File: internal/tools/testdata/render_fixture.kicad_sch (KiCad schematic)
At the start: 3 parts

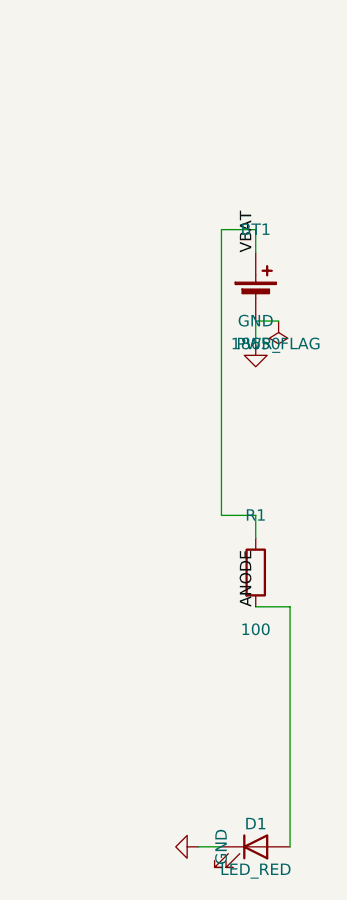
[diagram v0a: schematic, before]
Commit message: Prune projects/ down to the live compiled corpus
The F4 cutover retired the algorithmic pipeline but left its output
behind: 24 project directories from May and July whose only producer no
longer exists. What survives is projects/compiled_* — the seven
reference circuits built from docs/compiler/*.design.json — plus the
gitignored *_e2e output of verify_e2e.

Two tests were reading fixtures out of that rubble and would have gone
silently green via t.Skip once it was gone. TestRenderSchematicPNG now
uses internal/tools/testdata/render_fixture.kicad_sch instead of
projects/inv_amp_v2; TestBodyBBoxNeverSwallowsAPin keeps globbing
compiled_*, which is why that directory stays versioned.

Both verified to run rather than skip.

Co-Authored-By: Claude Opus 5 (1M context) <noreply@anthropic.com>
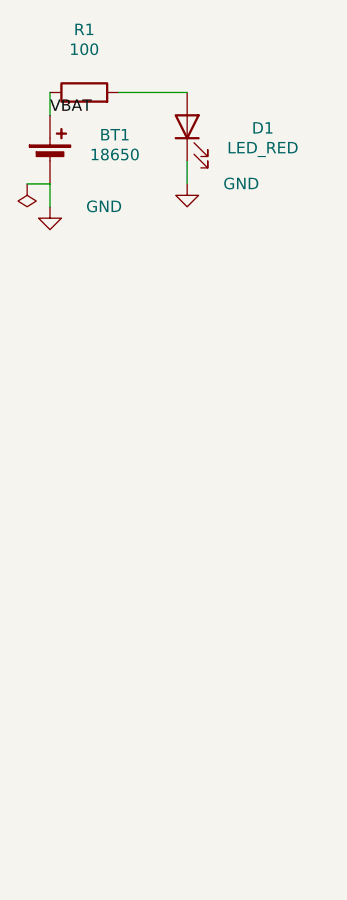
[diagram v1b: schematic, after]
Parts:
- BT1: footprint Battery:BatteryHolder_Keystone_1042_1x18650 -> (none)
- D1: footprint LED_THT:LED_D5.0mm -> (none)
- R1: footprint Resistor_THT:R_Axial_DIN0207_L6.3mm_D2.5mm_P7.62mm_Horizontal -> (none)
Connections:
- net ANODE: no longer names the net of D1.2 (A), R1.2
